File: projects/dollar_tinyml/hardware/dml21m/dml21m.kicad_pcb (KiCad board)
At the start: 2 copper layers, 30 x 12 mm, 31 parts, among them J2 Conn_ARM_SWD_TagConnect_TC203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, J4 Header 2.54mm, J5 USB_C_Receptacle_PowerOnly_6P, Q1 BC547B, SW1 PTS647SM50SMTR2LFS, U1 LIS2DH12, U2 Li charger 4054, U3 PY32F003F18U6TR, U4 XC6206P332MR

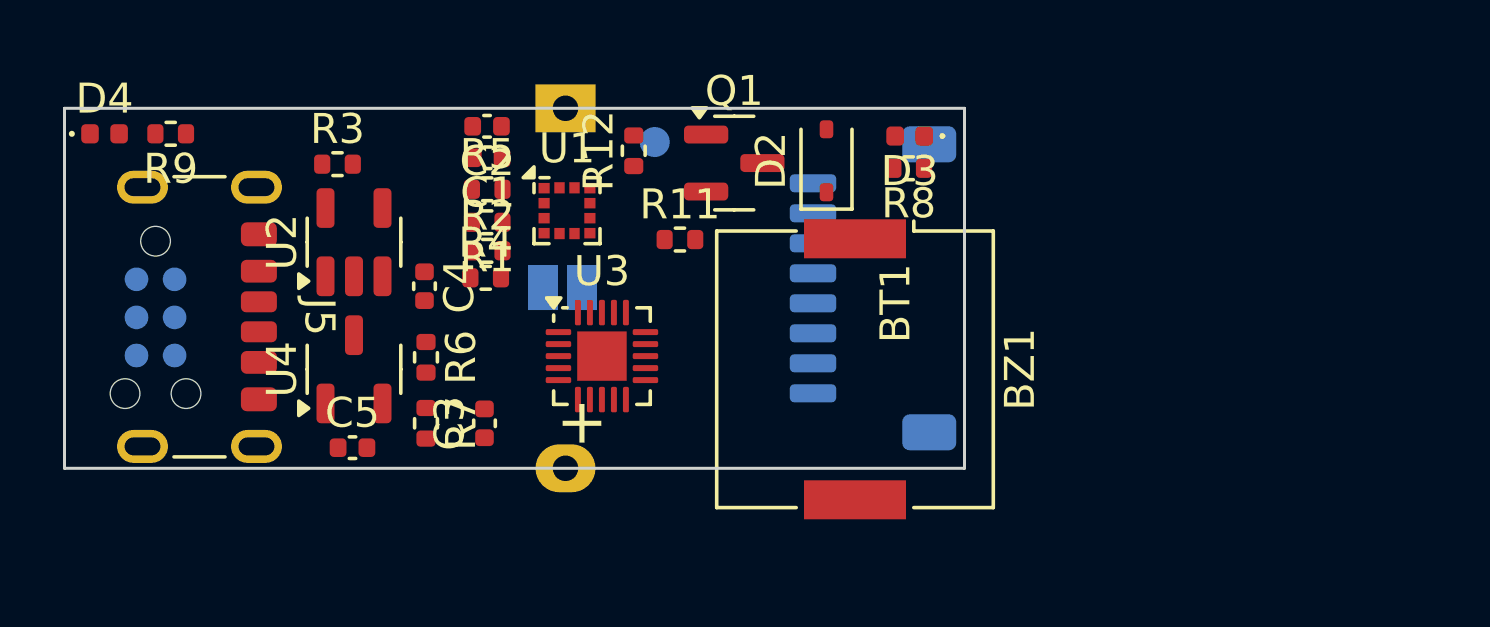
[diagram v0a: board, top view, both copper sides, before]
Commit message: dollarml: Try make PCB longer and flat
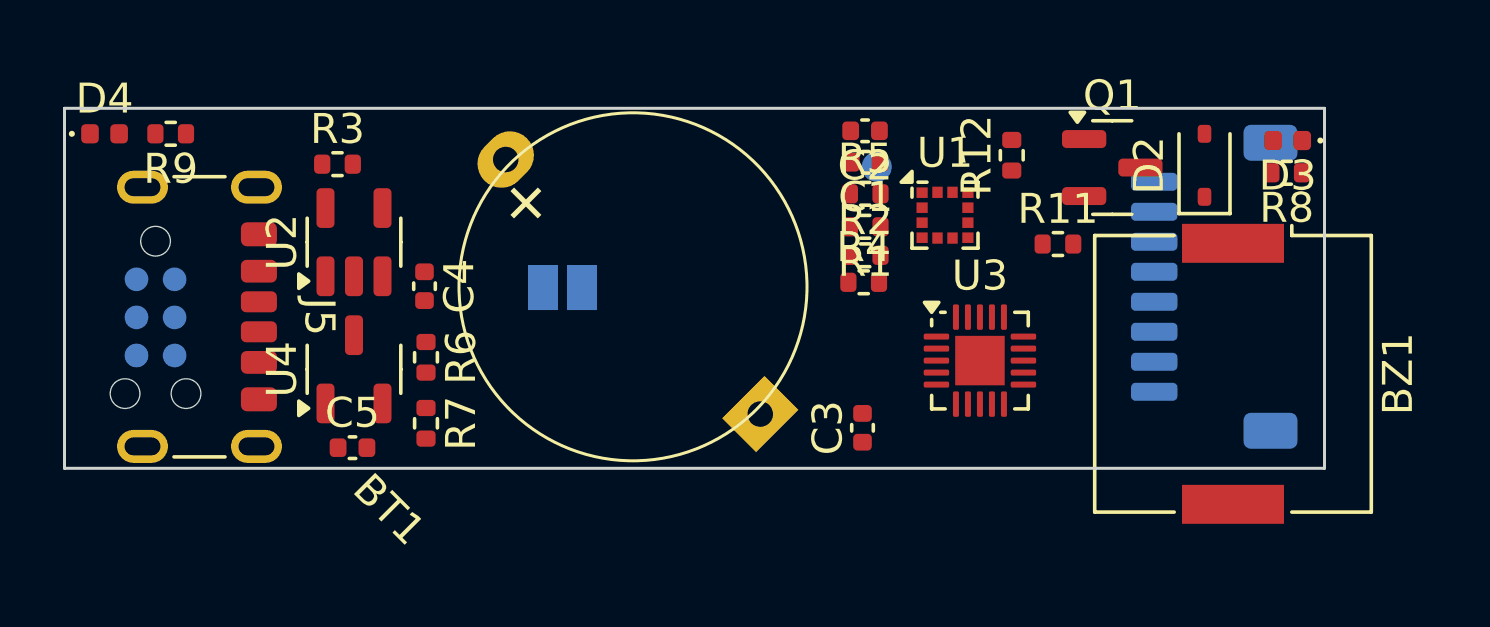
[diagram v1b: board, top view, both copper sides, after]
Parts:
- BT1: footprint dml20m:Battery_CR1220-Horizontal -> dml21m:Battery_CR1220-Horizontal
- moved C3 12.6 mm to (126.7, 104.7)
- moved D2 12.6 mm to (138.1, 96.0)
- moved U1 12.6 mm to (129.4, 97.6)
- moved BZ1 12.6 mm to (139.0, 102.9)
- moved C1 12.6 mm to (126.8, 95.8)
- moved C2 12.6 mm to (126.7, 94.8)
- moved D3 12.6 mm to (140.8, 95.1)
- moved Q1 12.6 mm to (135.0, 96.0)
- moved R1 12.6 mm to (126.7, 98.0)
- moved R11 12.6 mm to (133.2, 98.6)
- moved R12 12.6 mm to (131.6, 95.6)
- moved R2 12.6 mm to (126.7, 99.0)
- moved R4 12.6 mm to (126.7, 99.8)
- moved R5 12.6 mm to (126.7, 96.9)
- moved R8 12.6 mm to (140.8, 96.2)
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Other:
- board size 30 x 12 mm -> 42 x 12 mm
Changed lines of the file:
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@@
 	(footprint "Diode_SMD:D_SOD-323"
 		(layer "F.Cu")
-		(at 125.45 95.8 90)
+		(at 138.05 95.95 90)
 		(descr "SOD-323")
 		(tags "SOD-323")
@@
 	(footprint "Buzzer_Beeper:Buzzer_Murata_PKMCS0909E"
 		(layer "F.Cu")
-		(at 126.4 102.75 -90)
+		(at 139 102.9 -90)
 		(descr "Murata Buzzer http://www.murata.com/en-us/api/pdfdownloadapi?cate=&partno=PKMCS0909E4000-R1")
 		(tags "Murata Buzzer Beeper")
@@
 	(footprint "Capacitor_SMD:C_0402_1005Metric"
 		(layer "F.Cu")
-		(at 114.05 104.55 90)
+		(at 126.65 104.7 90)
 		(descr "Capacitor SMD 0402 (1005 Metric), square (rectangular) end terminal, IPC_7351 nominal, (Body size source: IPC-SM-782 page 76, https://www.pcb-3d.com/wordpress/wp-content/uploads/ipc-sm-782a_amendment_1_and_2.pdf), generated with kicad-footprint-generator")
 		(tags "capacitor")
@@
 	(footprint "Resistor_SMD:R_0402_1005Metric"
 		(layer "F.Cu")
-		(at 119.025 95.465 90)
+		(at 131.625 95.615 90)
 		(descr "Resistor SMD 0402 (1005 Metric), square (rectangular) end terminal, IPC_7351 nominal, (Body size source: IPC-SM-782 page 72, https://www.pcb-3d.com/wordpress/wp-content/uploads/ipc-sm-782a_amendment_1_and_2.pdf), generated with kicad-footprint-generator")
 		(tags "resistor")
@@
 	(footprint "Package_LGA:LGA-12_2x2mm_P0.5mm"
 		(layer "F.Cu")
-		(at 116.8 97.4625)
+		(at 129.4 97.6125)
 		(descr "LGA12")
 		(tags "lga land grid array")
@@
 	(footprint "Resistor_SMD:R_0402_1005Metric"
 		(layer "F.Cu")
-		(at 114.09 99.7)
+		(at 126.69 99.85)
 		(descr "Resistor SMD 0402 (1005 Metric), square (rectangular) end terminal, IPC_7351 nominal, (Body size source: IPC-SM-782 page 72, https://www.pcb-3d.com/wordpress/wp-content/uploads/ipc-sm-782a_amendment_1_and_2.pdf), generated with kicad-footprint-generator")
 		(tags "resistor")
@@
 	(footprint "Capacitor_SMD:C_0402_1005Metric"
 		(layer "F.Cu")
-		(at 114.135 94.65 180)
+		(at 126.735 94.8 180)
 		(descr "Capacitor SMD 0402 (1005 Metric), square (rectangular) end terminal, IPC_7351 nominal, (Body size source: IPC-SM-782 page 76, https://www.pcb-3d.com/wordpress/wp-content/uploads/ipc-sm-782a_amendment_1_and_2.pdf), generated with kicad-footprint-generator")
 		(tags "capacitor")
@@
 	(footprint "Capacitor_SMD:C_0402_1005Metric"
 		(layer "F.Cu")
-		(at 114.155 95.7 180)
+		(at 126.755 95.85 180)
 		(descr "Capacitor SMD 0402 (1005 Metric), square (rectangular) end terminal, IPC_7351 nominal, (Body size source: IPC-SM-782 page 76, https://www.pcb-3d.com/wordpress/wp-content/uploads/ipc-sm-782a_amendment_1_and_2.pdf), generated with kicad-footprint-generator")
 		(tags "capacitor")
@@
 	(footprint "Resistor_SMD:R_0402_1005Metric"
 		(layer "F.Cu")
-		(at 128.19 96.05 180)
+		(at 140.79 96.2 180)
 		(descr "Resistor SMD 0402 (1005 Metric), square (rectangular) end terminal, IPC_7351 nominal, (Body size source: IPC-SM-782 page 72, https://www.pcb-3d.com/wordpress/wp-content/uploads/ipc-sm-782a_amendment_1_and_2.pdf), generated with kicad-footprint-generator")
 		(tags "resistor")
@@
 	(footprint "Resistor_SMD:R_0402_1005Metric"
 		(layer "F.Cu")
-		(at 114.14 98.8)
+		(at 126.74 98.95)
 		(descr "Resistor SMD 0402 (1005 Metric), square (rectangular) end terminal, IPC_7351 nominal, (Body size source: IPC-SM-782 page 72, https://www.pcb-3d.com/wordpress/wp-content/uploads/ipc-sm-782a_amendment_1_and_2.pdf), generated with kicad-footprint-generator")
 		(tags "resistor")
@@
 	(footprint "LED_SMD:LED_0402_1005Metric"
 		(layer "F.Cu")
-		(at 128.2225 94.975 180)
+		(at 140.8225 95.125 180)
 		(descr "LED SMD 0402 (1005 Metric), square (rectangular) end terminal, IPC_7351 nominal, (Body size source: http://www.tortai-tech.com/upload/download/2011102023233369053.pdf), generated with kicad-footprint-generator")
 		(tags "LED")
@@
 	(footprint "Resistor_SMD:R_0402_1005Metric"
 		(layer "F.Cu")
-		(at 114.14 96.75)
+		(at 126.74 96.9)
 		(descr "Resistor SMD 0402 (1005 Metric), square (rectangular) end terminal, IPC_7351 nominal, (Body size source: IPC-SM-782 page 72, https://www.pcb-3d.com/wordpress/wp-content/uploads/ipc-sm-782a_amendment_1_and_2.pdf), generated with kicad-footprint-generator")
 		(tags "resistor")
@@
 	(footprint "Package_TO_SOT_SMD:SOT-23"
 		(layer "F.Cu")
-		(at 122.375 95.875)
+		(at 134.975 96.025)
 		(descr "SOT, 3 Pin (https://www.jedec.org/system/files/docs/to-236h.pdf variant AB), generated with kicad-footprint-generator ipc_gullwing_generator.py")
 		(tags "SOT TO_SOT_SMD")
@@
 		)
 	)
-	(footprint "dml20m:Battery_CR1220-Horizontal"
+	(footprint "dml21m:Battery_CR1220-Horizontal"
 		(layer "F.Cu")
-		(at 116.75 100.05 -90)
+		(at 119 100 135)
 		(descr "Panasonic CR-2032/HFN battery, https://industrial.panasonic.com/cdbs/www-data/pdf2/AAA4000/AAA4000D166.PDF")
 		(tags "battery CR-2032 coin cell")
 		(property "Reference" "BT1"
-			(at 0.5 -11 90)
+			(at 0.5 -11 135)
 			(layer "F.SilkS")
 			(effects
@@
 		)
 		(property "Value" "LIR1225"
-			(at 0 11 90)
+			(at 0 11.000001 135)
 			(layer "F.Fab")
 			(effects
@@
 			)
 		)
-		(property "Footprint" "dml20m:Battery_CR1220-Horizontal"
-			(at -10.5 0 -90)
+		(property "Footprint" "dml21m:Battery_CR1220-Horizontal"
+			(at -10.5 0 135)
 			(unlocked yes)
 			(layer "F.Fab")
@@
 		)
 		(property "Datasheet" ""
-			(at -10.5 0 -90)
+			(at -10.5 0 135)
 			(unlocked yes)
 			(layer "F.Fab")
@@
 		)
 		(property "Description" ""
-			(at -10.5 0 -90)
+			(at -10.5 0 135)
 			(unlocked yes)
 			(layer "F.Fab")
@@
 		(sheetname "Root")
 		(sheetfile "dml21m.kicad_sch")
-		(attr through_hole exclude_from_bom dnp)
+		(attr through_hole)
 		(fp_circle
 			(center 0 0)
-			(end 8 0)
+			(end 5.8 0)
+			(stroke
+				(width 0.1)
+				(type default)
+			)
+			(fill none)
+			(layer "F.SilkS")
+		)
+		(fp_circle
+			(center 0 0)
+			(end 6 0)
 			(stroke
 				(width 0.1)
@@
 		)
 		(fp_text user "+"
-			(at 4.5 -0.5 90)
+			(at 4.5 -0.5 135)
 			(layer "F.SilkS")
 			(effects
@@
 			)
 		)
-		(fp_text user "${REFERENCE}"
-			(at 0 0 90)
+		(fp_text user "+"
+			(at 4.5 -0.5 135)
 			(layer "F.Fab")
 			(effects
 				(font
-					(size 1 1)
+					(size 1.5 1.5)
 					(thickness 0.15)
 				)
 			)
 		)
-		(fp_text user "+"
-			(at 4.5 -0.5 90)
+		(fp_text user "${REFERENCE}"
+			(at 0 0 135)
 			(layer "F.Fab")
 			(effects
 				(font
-					(size 1.5 1.5)
+					(size 1 1)
 					(thickness 0.15)
 				)
@@
 		)
 		(pad "1" thru_hole oval
-			(at 6 0 270)
+			(at 6 0 135)
 			(size 1.6 2)
 			(drill 0.85)
@@
 		)
 		(pad "2" thru_hole rect
-			(at -6 0 270)
+			(at -6 0 135)
 			(size 1.6 2)
 			(drill 0.85)
@@
 	(footprint "Resistor_SMD:R_0402_1005Metric"
 		(layer "F.Cu")
-		(at 114.14 97.85 180)
+		(at 126.74 98 180)
 		(descr "Resistor SMD 0402 (1005 Metric), square (rectangular) end terminal, IPC_7351 nominal, (Body size source: IPC-SM-782 page 72, https://www.pcb-3d.com/wordpress/wp-content/uploads/ipc-sm-782a_amendment_1_and_2.pdf), generated with kicad-footprint-generator")
 		(tags "resistor")
@@
 	(footprint "Package_DFN_QFN:QFN-20-1EP_3x3mm_P0.4mm_EP1.65x1.65mm"
 		(layer "F.Cu")
-		(at 117.965 102.31)
+		(at 130.565 102.46)
 		(descr "QFN, 20 Pin (https://www.analog.com/media/en/technical-documentation/data-sheets/3553fc.pdf#page=34), generated with kicad-footprint-generator ipc_noLead_generator.py")
 		(tags "QFN NoLead")
@@
 	(footprint "Resistor_SMD:R_0402_1005Metric"
 		(layer "F.Cu")
-		(at 120.565 98.425)
+		(at 133.165 98.575)
 		(descr "Resistor SMD 0402 (1005 Metric), square (rectangular) end terminal, IPC_7351 nominal, (Body size source: IPC-SM-782 page 72, https://www.pcb-3d.com/wordpress/wp-content/uploads/ipc-sm-782a_amendment_1_and_2.pdf), generated with kicad-footprint-generator")
 		(tags "resistor")
@@
 	(footprint "Connector_JST:JST_SH_SM08B-SRSS-TB_1x08-1MP_P1.00mm_Horizontal"
 		(layer "B.Cu")
-		(at 127 100.05 -90)
+		(at 138.375 100 -90)
 		(descr "JST SH series connector, SM08B-SRSS-TB (http://www.jst-mfg.com/product/pdf/eng/eSH.pdf), generated with kicad-footprint-generator")
 		(tags "connector JST SH horizontal")
@@
 	(footprint "TestPoint:TestPoint_Pad_D1.0mm"
 		(layer "B.Cu")
-		(at 119.725 95.175 180)
+		(at 127.125 96 180)
 		(descr "SMD pad as test Point, diameter 1.0mm")
 		(tags "test point SMD pad")
@@
 	(gr_rect
 		(start 100.05 94.05)
-		(end 130.05 106.05)
+		(end 142.05 106.05)
 		(stroke
 			(width 0.1)

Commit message: dollarml: More sketches on next board
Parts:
- added TP1: TP_PCB, TestPoint:TestPoint_Pad_D1.0mm, B.Cu at (121.8, 105.8)
- added U5: PUYA P25Q16SH-SSH-IT, Package_SO:SOIC-8_5.3x5.3mm_P1.27mm, B.Cu at (118.0, 102.2)
- added U6: BM7161, dml10:BM7161, B.Cu at (123.2, 100.4)
- BT1: footprint dml21m:Battery_CR1220-Horizontal -> dml20m:Battery_CR1220-Horizontal
- moved J4 27.5 mm to (110.9, 100.0), turned to 90 degrees
- moved BT1 17.1 mm to (136.1, 100.5), turned to 90 degrees
- moved C3 11.8 mm to (114.8, 104.7)
- moved D2 11.8 mm to (126.2, 96.0)
- moved U1 11.8 mm to (117.6, 97.6)
- moved BZ1 11.8 mm to (127.2, 102.9)
- moved C1 11.8 mm to (115.0, 95.8)
- moved C2 11.8 mm to (114.9, 94.8)
- moved Q1 11.8 mm to (123.2, 96.0)
- moved R1 11.8 mm to (114.9, 98.0)
- moved R11 11.8 mm to (121.4, 98.6)
- moved R12 11.8 mm to (119.8, 95.6)
- moved R2 11.8 mm to (114.9, 99.0)
- moved R5 11.8 mm to (114.9, 96.9)
- moved U3 11.8 mm to (118.8, 102.5)
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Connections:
- J4 pad 1: /SWCLK -> /RESET
- J4 pad 2: VDD -> /SWCLK
- J4 pad 3: GND -> VDD
- J4 pad 4: /SDA -> GND
- J4 pad 5: /SCL -> /SDA
- J4 pad 6: /SWDIO -> /SCL
- J4 pad 7: (no net) -> /SWDIO
- J4 pad 8: (no net) -> unconnected-(J4-Pin_8-Pad8)
- U3 pad 3: /LED_RED_P -> unconnected-(U3-PA7-Pad3)
- U3 pad 5: /LED_BLUE_P -> unconnected-(U3-PA12-Pad5)
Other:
- board size 42 x 12 mm -> 42 x 14.2 mm
